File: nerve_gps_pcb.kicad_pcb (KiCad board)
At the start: 4 copper layers, 50 x 50 mm, 14 parts, among them J1 2x8, J2 WS2812B, J3 5V GPIO Breakout, U1 SAM-M10Q, U2 TXB0104QPWRQ1

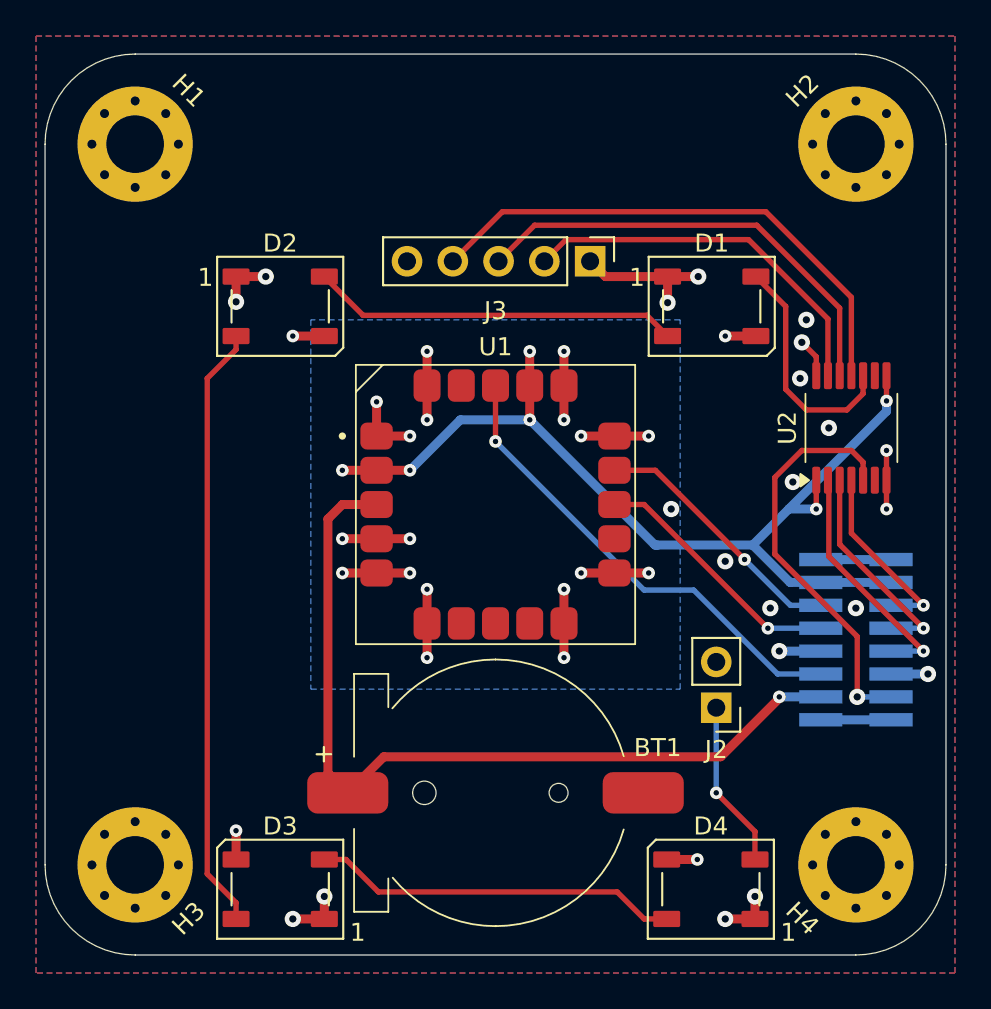
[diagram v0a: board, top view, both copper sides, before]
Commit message: Add ground stitching vias and silkscreen cleanup
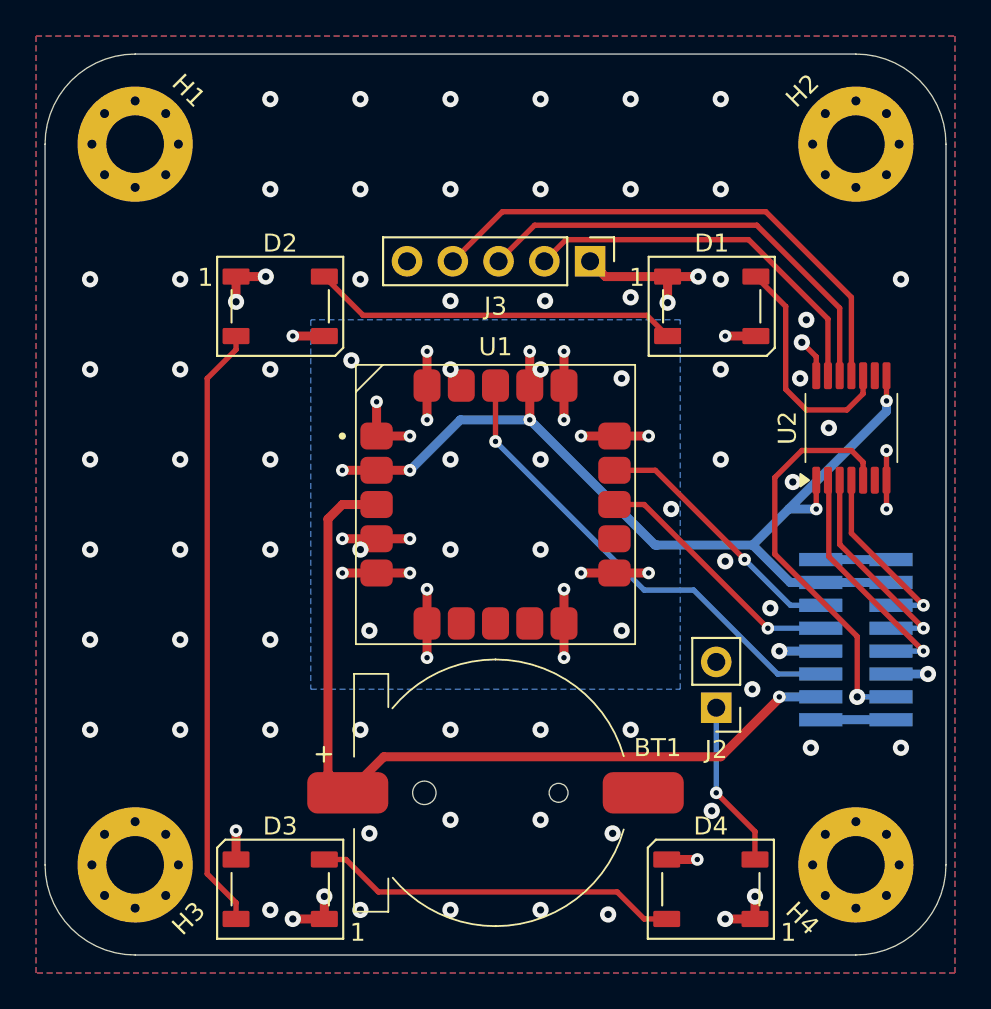
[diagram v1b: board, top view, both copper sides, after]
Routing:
- net GND: vias 34 -> 98

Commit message: Fix bad vias
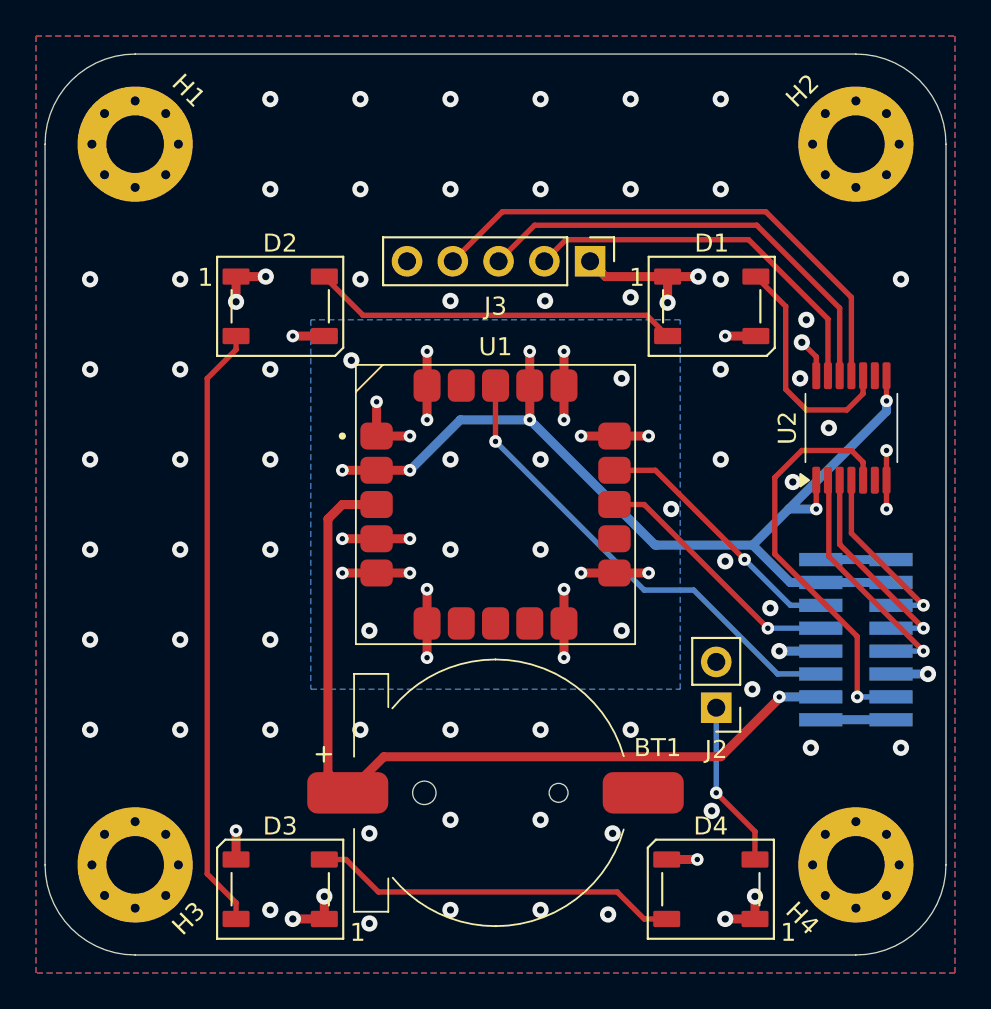
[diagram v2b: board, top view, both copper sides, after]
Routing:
- net GND: vias 98 -> 95
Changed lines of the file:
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@@
-	)
-	(via
-		(at 151 97.5)
-		(size 0.9)
-		(drill 0.4)
-		(layers "F.Cu" "B.Cu")
-		(free yes)
-		(net 2)
 	)
 	(via
@@
 	)
 	(via
-		(at 141 127.5)
+		(at 141.5 128.25)
 		(size 0.9)
 		(drill 0.4)
@@
 	)
 	(via
-		(at 146 97.5)
-		(size 0.9)
-		(drill 0.4)
-		(layers "F.Cu" "B.Cu")
-		(free yes)
-		(net 2)
-	)
-	(via
 		(at 170.2 105.25)
 		(size 0.7)
@@
 	(via
 		(at 154.75 127.75)
-		(size 0.9)
-		(drill 0.4)
-		(layers "F.Cu" "B.Cu")
-		(free yes)
-		(net 2)
-	)
-	(via
-		(at 141 107.5)
 		(size 0.9)
 		(drill 0.4)
@@
 	)
 	(segment
+		(start 168.575 112.325)
+		(end 164 107.75)
+		(width 0.3)
+		(layer "F.Cu")
+		(net 10)
+	)
+	(segment
+		(start 168.25 102)
+		(end 168.9 102.65)
+		(width 0.3)
+		(layer "F.Cu")
+		(net 10)
+	)
+	(segment
+		(start 164 107.75)
+		(end 164 103.5)
+		(width 0.3)
+		(layer "F.Cu")
+		(net 10)
+	)
+	(segment
+		(start 165.5 102)
+		(end 168.25 102)
+		(width 0.3)
+		(layer "F.Cu")
+		(net 10)
+	)
+	(segment
+		(start 168.575 115.675)
+		(end 168.575 112.325)
+		(width 0.3)
+		(layer "F.Cu")
+		(net 10)
+	)
+	(segment
+		(start 164 103.5)
+		(end 165.5 102)
+		(width 0.3)
+		(layer "F.Cu")
+		(net 10)
+	)
+	(segment
 		(start 168.9 102.65)
 		(end 168.9 103.65)
@@
 		(net 10)
 	)
-	(segment
-		(start 168.575 115.675)
-		(end 168.575 112.325)
-		(width 0.3)
-		(layer "F.Cu")
+	(via
+		(at 168.575 115.675)
+		(size 0.7)
+		(drill 0.3)
+		(layers "F.Cu" "B.Cu")
 		(net 10)
-	)
-	(segment
-		(start 165.5 102)
-		(end 168.25 102)
-		(width 0.3)
-		(layer "F.Cu")
-		(net 10)
-	)
-	(segment
-		(start 168.575 112.325)
-		(end 164 107.75)
-		(width 0.3)
-		(layer "F.Cu")
-		(net 10)
-	)
-	(segment
-		(start 164 103.5)
-		(end 165.5 102)
-		(width 0.3)
-		(layer "F.Cu")
-		(net 10)
-	)
-	(segment
-		(start 168.25 102)
-		(end 168.9 102.65)
-		(width 0.3)
-		(layer "F.Cu")
-		(net 10)
-	)
-	(segment
-		(start 164 107.75)
-		(end 164 103.5)
-		(width 0.3)
-		(layer "F.Cu")
-		(net 10)
-	)
-	(via
-		(at 168.575 115.675)
-		(size 0.9)
-		(drill 0.4)
-		(layers "F.Cu" "B.Cu")
-		(net 10)

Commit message: Cleanup and update board-to-board connector
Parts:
- J1: value 2x8 -> BF080-16-A-1-L-C; footprint Connector_PinHeader_1.27mm:PinHeader_2x08_P1.27mm_Vertical_SMD -> connectors:bf080-16-a-1-l-c
- moved J2 24.6 mm to (170.8, 93.8)
- moved D3 10.3 mm to (136.5, 83.8), turned to 180 degrees
- moved D4 10.2 mm to (160.5, 83.8), turned to 180 degrees
- moved J1 0.90 mm to (169.2, 113.0), turned to -90 degrees
- moved D1 0.11 mm to (160.5, 126.2), turned to 0 degrees
- moved D2 0.11 mm to (136.5, 126.2), turned to 0 degrees
- renumbered D4 to D1, D3 to D2, D2 to D3, D1 to D4
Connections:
- D1 pad 2: Net-(D4-DOUT) -> Net-(D1-DOUT)
- D1 pad 4: Net-(D3-DOUT) -> /LED_PWM_{5V}
- D2 pad 2: Net-(D3-DOUT) -> Net-(D2-DOUT)
- D2 pad 4: Net-(D2-DOUT) -> Net-(D1-DOUT)
- D3 pad 2: Net-(D2-DOUT) -> Net-(D3-DOUT)
- D3 pad 4: Net-(D1-DOUT) -> Net-(D2-DOUT)
- D4 pad 2: Net-(D1-DOUT) -> Net-(D4-DOUT)
- D4 pad 4: /LED_PWM_{5V} -> Net-(D3-DOUT)
- J1 pad 13: /LED_PWM -> /LED_PWM_{5V}
- J1 pad 5: /GPIO_3 -> /GPIO_1
- J1 pad 9: /GPIO_1 -> /GPIO_3
- U2 pad 10: /LED_PWM_{5V} -> unconnected-(U2-B4-Pad10)
- U2 pad 5: /LED_PWM -> unconnected-(U2-A4-Pad5)
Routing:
- net /LED_PWM: track 22.7 -> 0.00 mm, vias 1 -> 0
- net +3V3: track 54.7 -> 38.8 mm, vias 6 -> 10
- net +5V: track 22.8 -> 12.7 mm, vias 9 -> 5
- net Net-(D2-DOUT): track 33.7 -> 43.6 mm
- net /GPIO_1: track 13.5 -> 6.47 mm
- net /GPS_UART_RX: track 14.3 -> 20.4 mm
- net /GPS_NRST: track 26.5 -> 32.4 mm
- net /GPS_UART_TX: track 14.6 -> 20.2 mm
- net Net-(D4-DOUT): track 9.32 -> 14.9 mm, vias 1 -> 0
- net +3.3VBATT: track 47.2 -> 52.5 mm
- net /LED_PWM_{5V}: track 13.1 -> 9.17 mm, vias 0 -> 1
- net GND: track 48.3 -> 45.1 mm, vias 95 -> 92
- net /GPIO_3: track 10.4 -> 12.5 mm
- net /GPIO_2: track 11.9 -> 10.1 mm
- net Net-(J1-Pad15): track 3.90 -> 5.00 mm
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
